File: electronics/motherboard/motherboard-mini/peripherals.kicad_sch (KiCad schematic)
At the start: 12 parts, among them J2 ST1W008S4AR1500, J4 2604-3105, Q3 BSS214NW, Q6 BSS214NW, U14 TCA9534

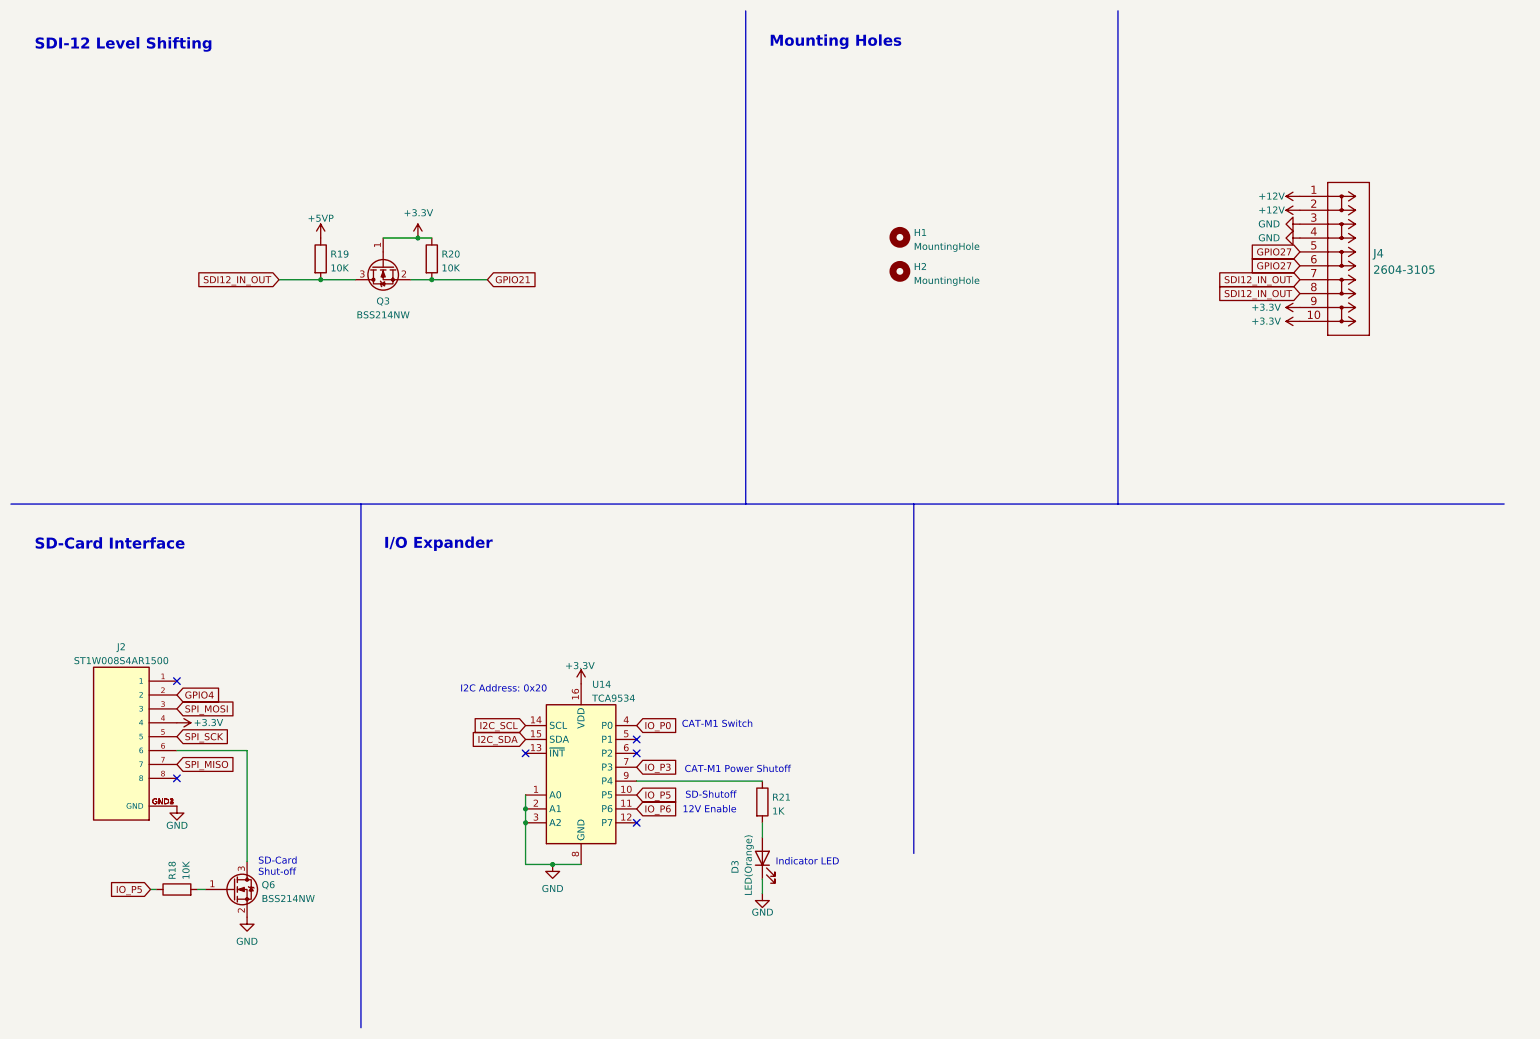
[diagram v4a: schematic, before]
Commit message: new version sent for manufacture, updated component positioning, removed level shifter on SDI-12 line, re routed the solar charge circuit
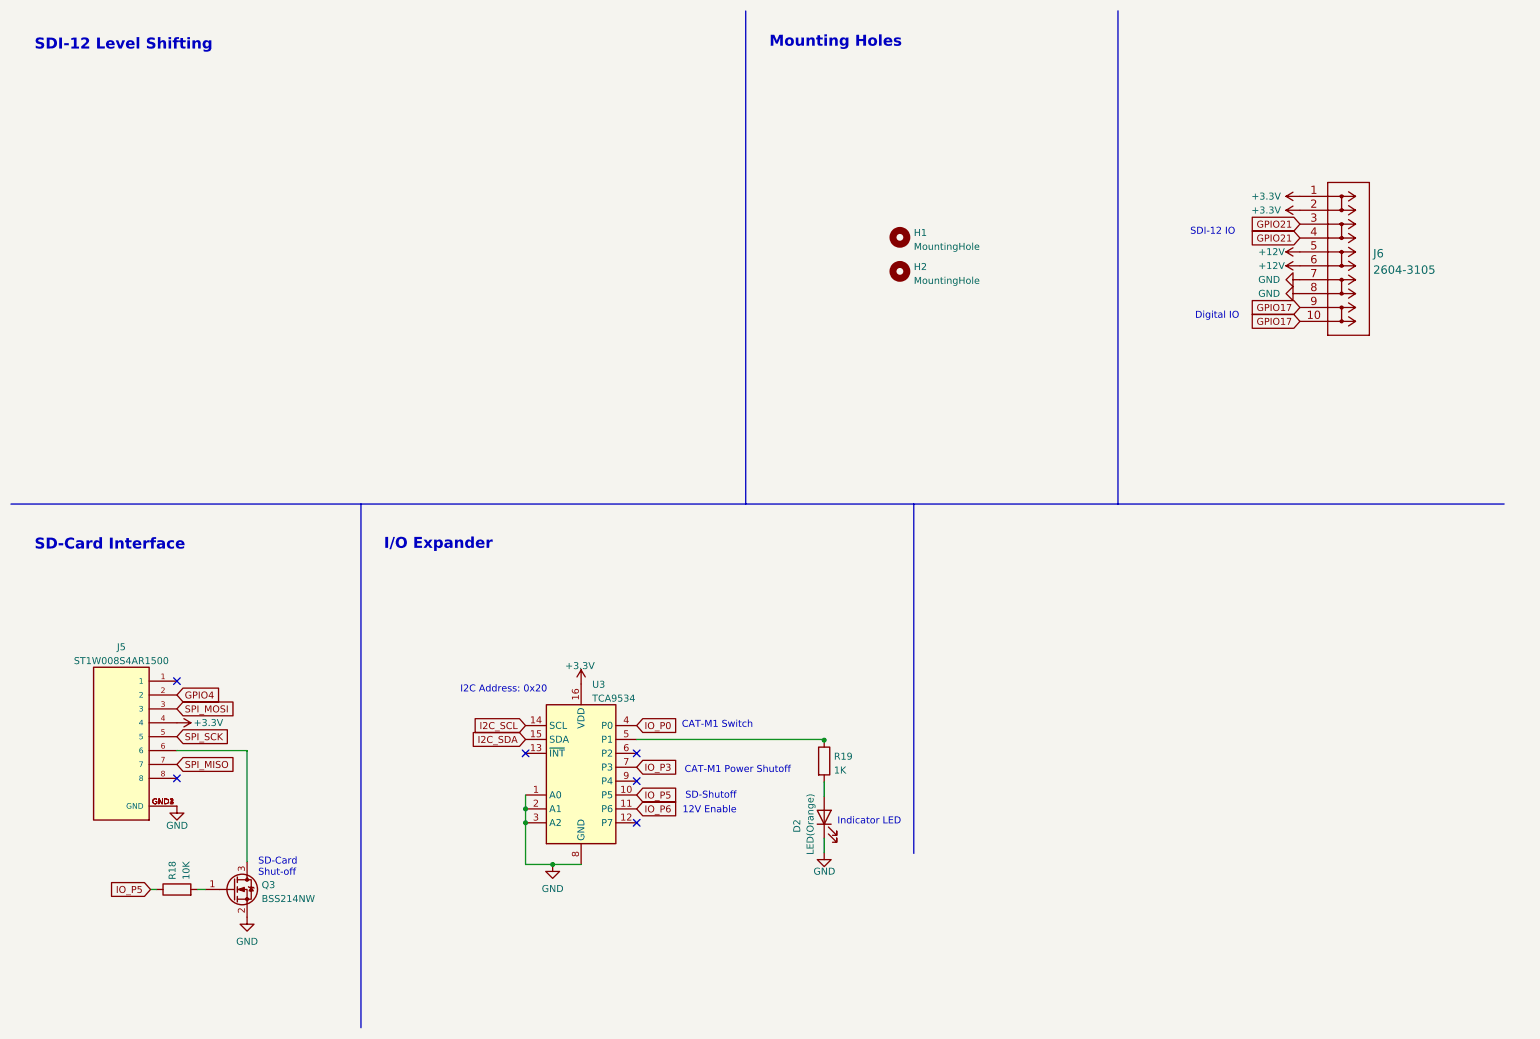
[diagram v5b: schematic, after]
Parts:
- removed Q3: BSS214NW, Package_TO_SOT_SMD:SOT-323_SC-70, symbol Transistor_FET:BSS214NW
- removed R19, R20: 10K, Resistor_SMD:R_0805_2012Metric, symbol Device:R
- renumbered D3 to D2, J2 to J5, J4 to J6, Q6 to Q3, R21 to R19, U14 to U3
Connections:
- net GPIO27 is gone; now on net +12V: J6.5, J6.6
- net SDI12_IN_OUT is gone; now on net GND: J6.7, J6.8
- net +12V: no longer J6.1, J6.2
- net +3.3V: now also J6.1, J6.2; no longer J6.10, J6.9
- net GND: no longer J6.3, J6.4
- net GPIO21: now also J6.3, J6.4
- net at U3.5 (P1): now also R19.1
- net at U3.9 (P4): no longer R19.1
- new net GPIO17: J6.10, J6.9
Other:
- note added: "Digital IO"
- note added: "SDI-12 IO"
- moved on the sheet: D2, R19

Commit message: refactored schemematics and added pdf previews for readme
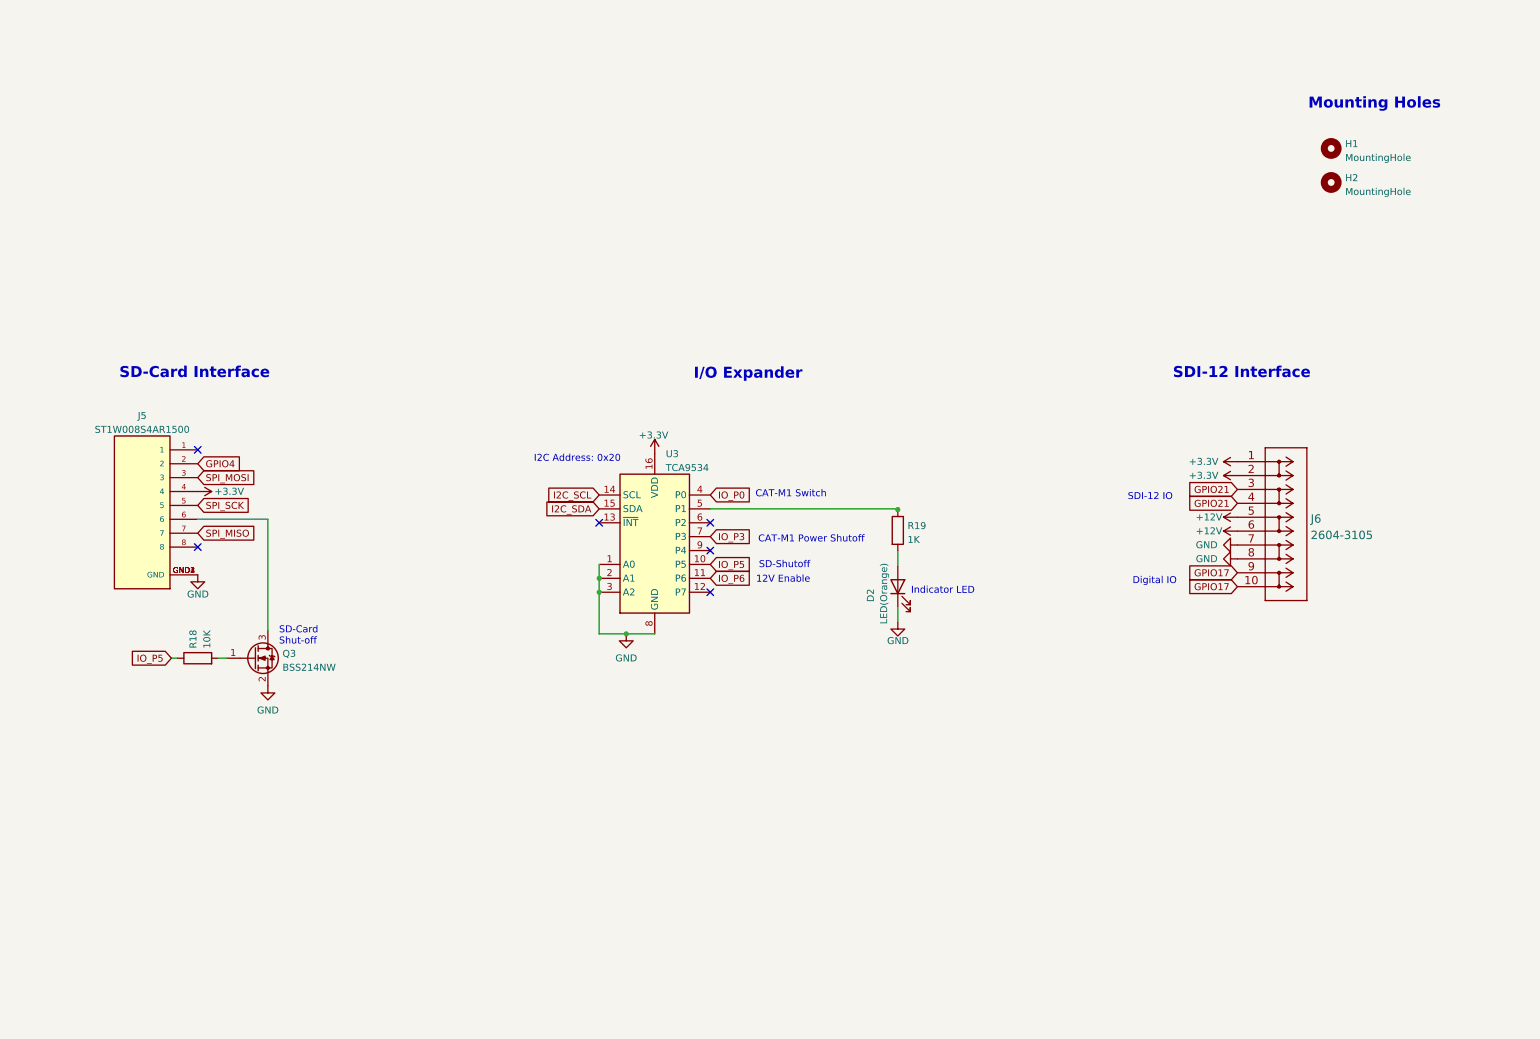
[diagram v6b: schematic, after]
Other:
- note added: "SDI-12 Interface"
- note removed: "SDI-12 Level Shifting"
- company: (none) -> NSW Department of Primary Industries
- title: (none) -> Enviro-node
- moved on the sheet: D2, H1, H2, J5, J6, Q3, R18, R19, U3
